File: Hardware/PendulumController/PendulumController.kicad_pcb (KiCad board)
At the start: 2 copper layers, 152 x 89 mm, 48 parts, among them J101 MOTOR, J102 ENCODER, J201 Tag Connect, J301 19V Input, J401 USB_B_Micro, J402 PROG, SW201 RESET, SW202 START_SW, SW203 STOP/MODE_SW, U201 ATmega328P-A, U301 NCV1117ST50T3G, U401 FT232RL, Y201 16mHz

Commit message: Cleanup board layout, cleanup firmware and go to bed, this is a sturdy place to start a new project!
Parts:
- added H101: PiMountingHole, MountingHole:MountingHole_2.7mm, F.Cu at (220.0, 70.0)
- added H102: PiMountingHole, MountingHole:MountingHole_2.7mm, F.Cu at (145.0, 110.0)
- added H103: PiMountingHole, MountingHole:MountingHole_2.7mm, F.Cu at (145.0, 70.0)
- added H104: PiMountingHole, MountingHole:MountingHole_2.7mm, F.Cu at (220.0, 110.0)
- added H105: PiMountingHole, MountingHole:MountingHole_2.7mm, F.Cu at (70.0, 70.0)
- added H106: PiMountingHole, MountingHole:MountingHole_2.7mm, F.Cu at (70.0, 110.0)
- J201: value Tag Connect -> ICSP
- U201: value ATmega328P-A -> ATmega328P
- moved R208 85.9 mm to (75.8, 84.2)
- moved SW201 85.6 mm to (89.5, 81.8)
- moved SW203 85.6 mm to (78.9, 81.8)
- moved R207 83.6 mm to (96.6, 84.0)
- moved SW202 81.7 mm to (99.8, 81.8)
- moved C404 74.3 mm to (163.0, 77.5)
- moved R206 71.5 mm to (86.2, 84.0)
- moved R403 67.1 mm to (193.8, 73.8), turned to 90 degrees
- moved J102 66.7 mm to (152.2, 108.7)
- moved D401 65.9 mm to (193.8, 70.2), turned to 90 degrees
- moved R301 65.3 mm to (198.5, 102.5)
- moved JP401 63.1 mm to (197.8, 71.0), turned to 90 degrees
- moved R404 63.1 mm to (190.5, 73.8), turned to -90 degrees
- moved G*** 62.8 mm to (135.5, 107.5)
- moved REF** 62.8 mm to (125.5, 108.5)
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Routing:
- added copper zone on B.Cu, net GND
- added copper zone on F.Cu, net GND
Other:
- board size 152 x 89 mm -> 157 x 47 mm

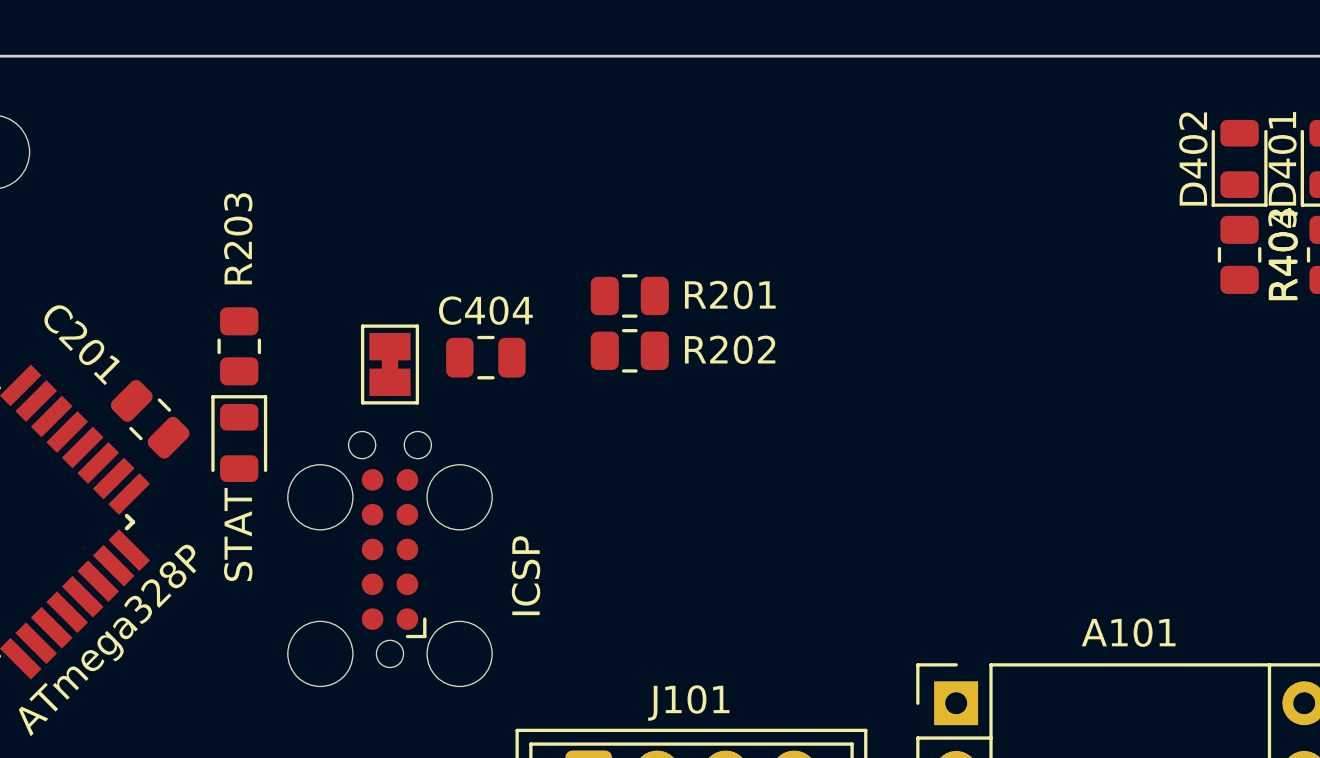
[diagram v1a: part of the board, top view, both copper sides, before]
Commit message: Add TFT connector
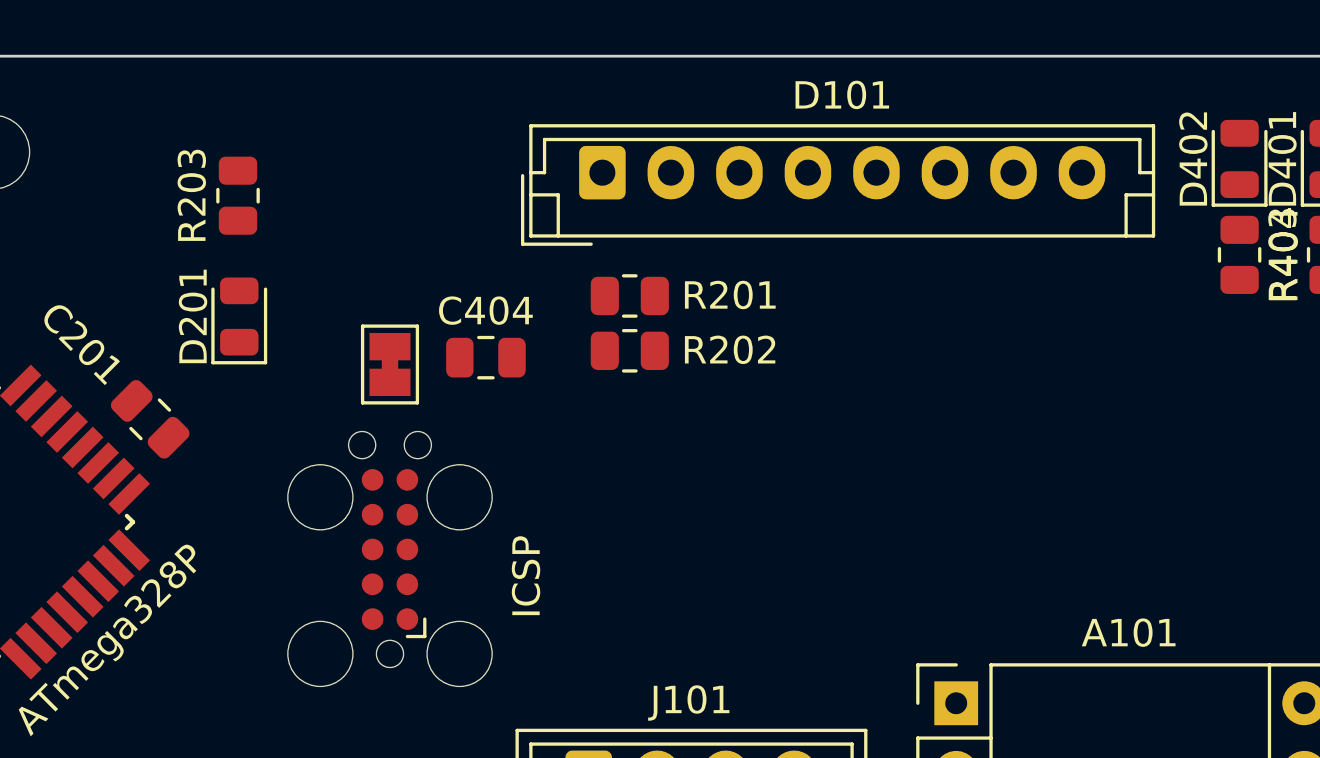
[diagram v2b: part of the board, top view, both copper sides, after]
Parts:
- added D101: 1.8TFT, Connector_JST:JST_EH_B8B-EH-A_1x08_P2.50mm_Vertical, F.Cu at (167.2, 70.8)
- moved R203 5.50 mm to (154.0, 71.6), turned to 90 degrees
- moved D201 4.61 mm to (154.0, 76.0), turned to 90 degrees
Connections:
- net /MCU/ICSP_MISO renamed /MCU/SDI
- net /MCU/ICSP_MOSI renamed /MCU/SDO
- net /MCU/ICSP_SCK renamed /MCU/SCK

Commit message: Add stencil cutouts and bump kicad libs
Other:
- board text added: "Stencil Size"
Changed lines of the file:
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@@
   (gr_line (start 70 113.5) (end 220 113.5) (layer "Edge.Cuts") (width 0.1))
   (gr_line (start 223.5 110) (end 223.5 70) (layer "Edge.Cuts") (width 0.1))
+  (gr_rect (start 55 55) (end 235 135) (layer "F.Fab") (width 0.1) (fill none))
   (gr_text "Inverted Pendulum Controller Board\n${FULL_REVISION}" (at 68.5 93.5) (layer "F.SilkS")
     (effects (font (size 2 2) (thickness 0.4)) (justify left))
@@
     (effects (font (size 1 1) (thickness 0.15)))
   )
+  (gr_text "Stencil\nSize" (at 50 50) (layer "F.Fab")
+    (effects (font (size 1 1) (thickness 0.15)))
+  )
+  (dimension (type aligned) (layer "F.Fab")
+    (pts (xy 235 55) (xy 55 55))
+    (height 4.999999)
+    (gr_text "180.0000 mm" (at 145 48.850001) (layer "F.Fab")
+      (effects (font (size 1 1) (thickness 0.15)))
+    )
+    (format (units 3) (units_format 1) (precision 4))
+    (style (thickness 0.1) (arrow_length 1.27) (text_position_mode 0) (extension_height 0.58642) (extension_offset 0.5) keep_text_aligned)
+  )
+  (dimension (type aligned) (layer "F.Fab")
+    (pts (xy 55 55) (xy 55 135))
+    (height 5)
+    (gr_text "80.0000 mm" (at 48.85 95 90) (layer "F.Fab")
+      (effects (font (size 1 1) (thickness 0.15)))
+    )
+    (format (units 3) (units_format 1) (precision 4))
+    (style (thickness 0.1) (arrow_length 1.27) (text_position_mode 0) (extension_height 0.58642) (extension_offset 0.5) keep_text_aligned)
+  )
   (zone (net 1) (net_name "GND") (layers F&B.Cu) (hatch edge 0.508)

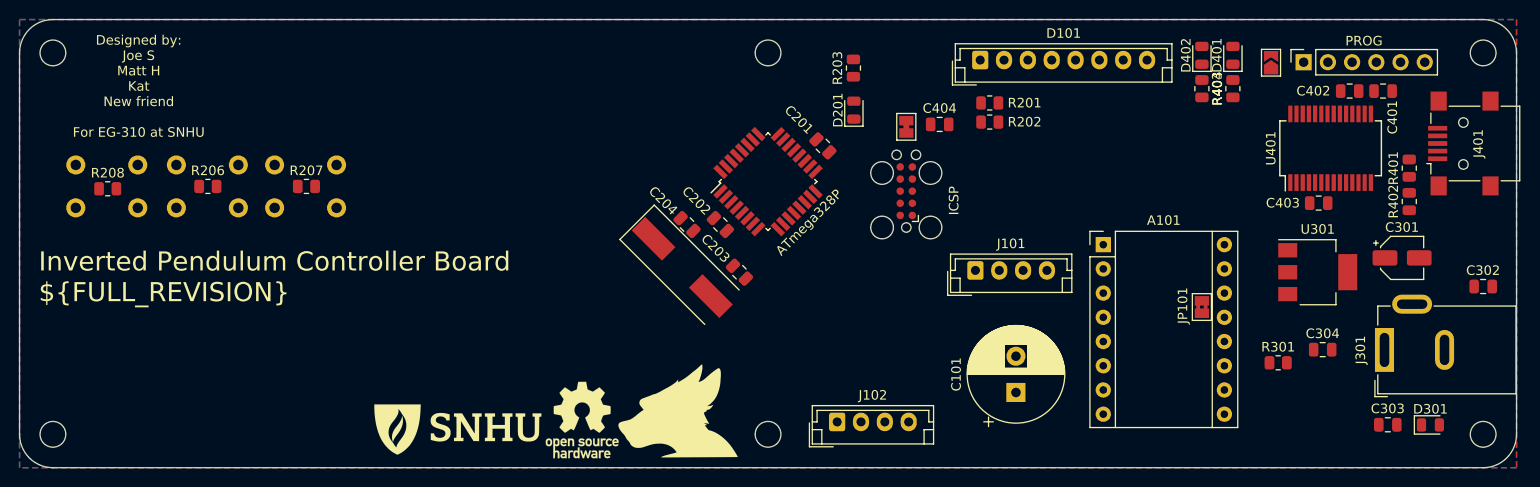
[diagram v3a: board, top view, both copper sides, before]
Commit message: Clean up board design with embedded power supply
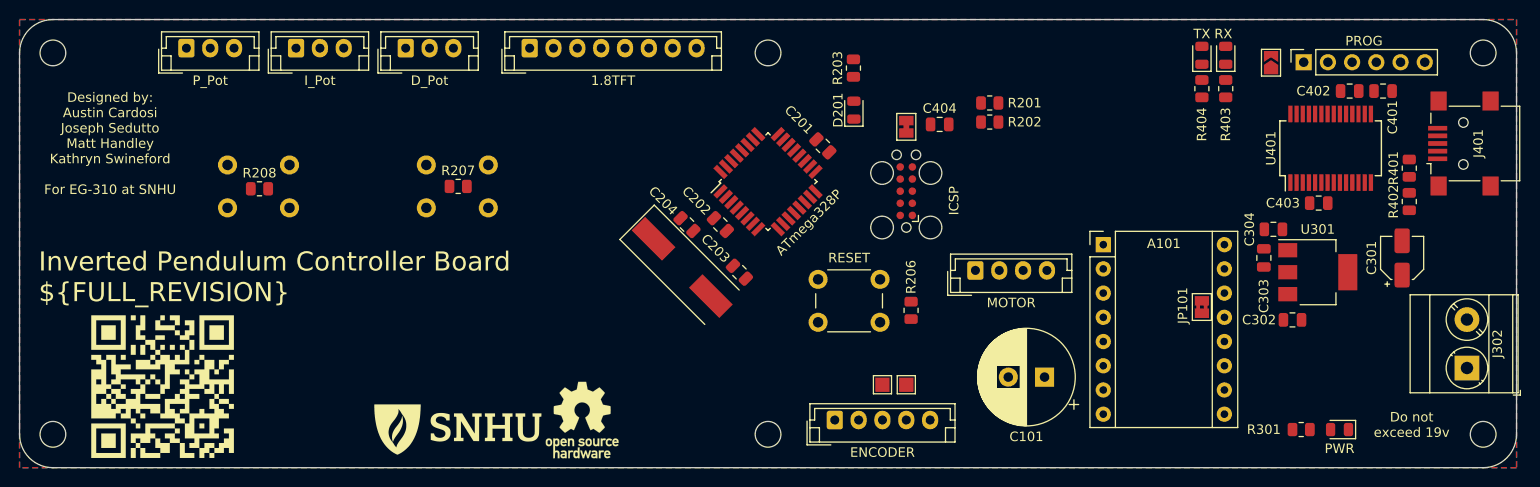
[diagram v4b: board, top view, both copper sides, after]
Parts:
- removed G***: LOGO, KenwoodFox:KITSUNE_LOGO
- removed J301: 19V Input, Connector_BarrelJack:BarrelJack_GCT_DCJ200-10-A_Horizontal
- added J302: 19V Input, TerminalBlock_Phoenix:TerminalBlock_Phoenix_MKDS-3-2-5.08_1x02_P5.08mm_Horizontal, F.Cu at (218.3, 103.0)
- added QRCODE: LOGO, Misc:custom_silkscreen, F.Cu at (81.5, 105.0)
- added RV201: P_Pot, Connector_JST:JST_EH_B3B-EH-A_1x03_P2.50mm_Vertical, F.Cu at (84.0, 69.5)
- added RV202: I_Pot, Connector_JST:JST_EH_B3B-EH-A_1x03_P2.50mm_Vertical, F.Cu at (95.5, 69.5)
- added RV203: D_Pot, Connector_JST:JST_EH_B3B-EH-A_1x03_P2.50mm_Vertical, F.Cu at (107.0, 69.5)
- added TP101: TestPoint, TestPoint:TestPoint_Pad_1.5x1.5mm, F.Cu at (159.5, 104.8)
- added TP102: TestPoint, TestPoint:TestPoint_Pad_1.5x1.5mm, F.Cu at (157.0, 104.8)
- J102: footprint Connector_JST:JST_EH_B4B-EH-A_1x04_P2.50mm_Vertical -> Connector_JST:JST_EH_B5B-EH-A_1x05_P2.50mm_Vertical
- SW201: moved to F.Cu
- moved R206 74.9 mm to (160.0, 97.0), turned to 90 degrees
- moved SW201 62.0 mm to (150.2, 93.8), turned to 0 degrees
- moved D101 47.3 mm to (120.0, 69.5)
- moved C303 21.8 mm to (197.0, 91.5), turned to 90 degrees
- moved C302 20.3 mm to (200.0, 98.0)
- moved R207 15.9 mm to (112.5, 84.0)
- moved R208 15.9 mm to (91.7, 84.2)
- moved SW202 15.9 mm to (115.7, 81.8)
- moved SW203 15.9 mm to (94.8, 81.8)
- moved C304 13.6 mm to (198.0, 88.5)
- moved D301 9.54 mm to (204.9, 109.5), turned to 180 degrees
- moved R301 7.40 mm to (200.9, 109.5)
- moved C101 3.40 mm to (174.0, 104.0), turned to 180 degrees
- moved D401 0.75 mm to (193.0, 70.2)
- moved R403 0.75 mm to (193.0, 73.8)
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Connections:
- D101 pad 3: unconnected-(D101-Pad3) -> /MCU/TFT_CS
- D101 pad 4: unconnected-(D101-Pad4) -> /MCU/TFT_RESET
- D101 pad 5: unconnected-(D101-Pad5) -> /MCU/TFT_A0
- D101 pad 6: unconnected-(D101-Pad6) -> /MCU/SDO
- D101 pad 7: unconnected-(D101-Pad7) -> /MCU/SCK
- J102 pad 2: /SCL -> GND
- J102 pad 3: /SDA -> /EncA
- J102 pad 4: +5V -> /EncB
- U201 pad 1: /MCU/STOP/MODE -> /EncB
- U201 pad 10: unconnected-(U201-Pad10) -> /MCU/TFT_A0
- U201 pad 11: unconnected-(U201-Pad11) -> /MCU/STOP/MODE
- U201 pad 14: unconnected-(U201-Pad14) -> /MCU/START
- U201 pad 2: unconnected-(U201-Pad2) -> /MCU/TFT_RESET
- U201 pad 32: /MCU/START -> /EncA
- U201 pad 9: unconnected-(U201-Pad9) -> /MCU/TFT_CS
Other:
- board text added: "Designed by: Austin Cardosi Joseph Sedutto Matt Handley Kathryn Swineford For EG-310 at SNHU"
- board text added: "Do not exceed 19v"
- board text removed: "Designed by: Joe S Matt H Kat New friend For EG-310 at SNHU"
